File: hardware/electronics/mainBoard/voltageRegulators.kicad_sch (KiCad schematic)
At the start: 35 parts, among them U14 TPS65268-Q1

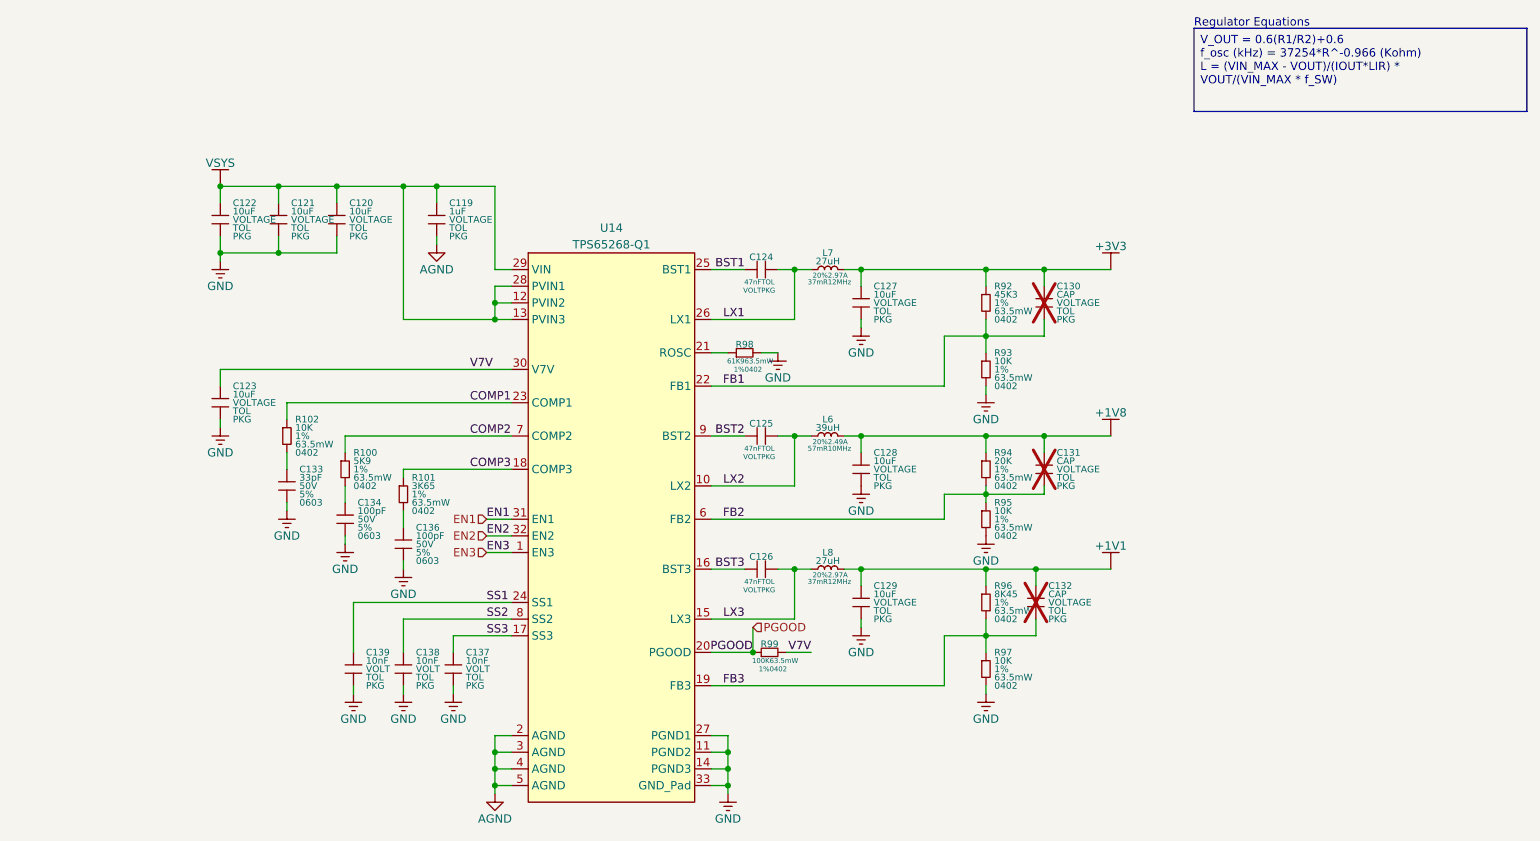
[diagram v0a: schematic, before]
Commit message: fixed vreg from WEBENCH results
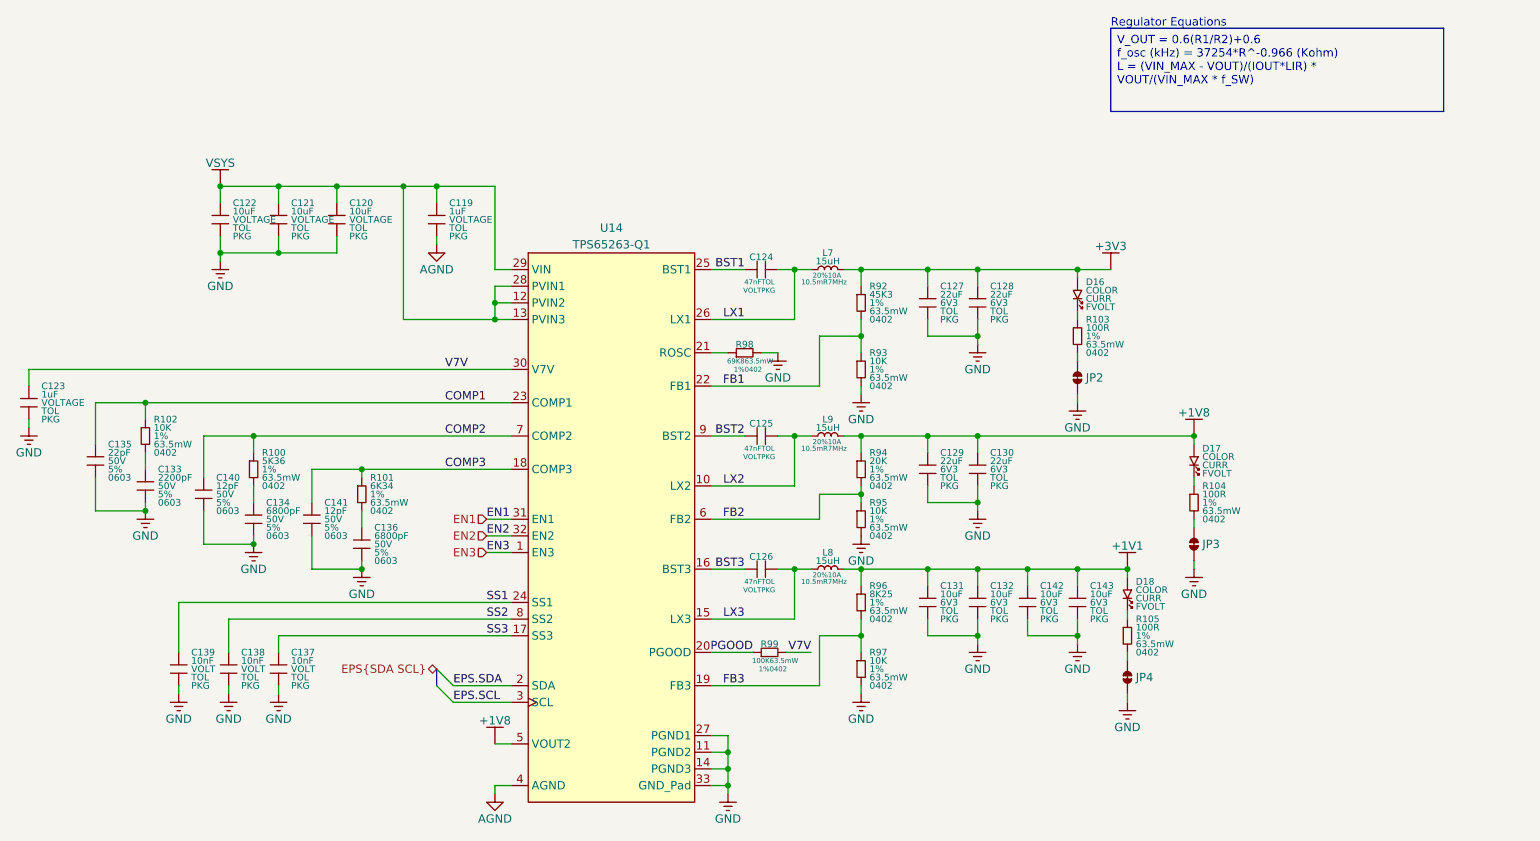
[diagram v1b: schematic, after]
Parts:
- removed L6: 39uH, symbol lib_sch:L_horizontal
- removed U14: TPS65268-Q1, symbol lib_sch:TPS65268-Q1
- added C135: 22pF, symbol lib_sch:C
- added C140, C141: 12pF, symbol lib_sch:C
- added C142, C143: 10uF, symbol lib_sch:C
- added D16, D17, D18: ~, symbol lib_sch:LED
- added JP2, JP3, JP4: ~, symbol .DS-Jumpers:Jumper_2_Bridged
- added L9: 15uH, symbol lib_sch:L_horizontal
- added R103, R104, R105: 100R, symbol lib_sch:R
- added U14: TPS65263-Q1, symbol lib_sch:TPS65263-Q1
- C123: value 10uF -> 1uF
- C127, C128, C129: value 10uF -> 22uF; Voltage Rating VOLTAGE -> 6V3
- C130: value CAP -> 22uF; Voltage Rating VOLTAGE -> 6V3; now fitted
- C131, C132: value CAP -> 10uF; Voltage Rating VOLTAGE -> 6V3; now fitted
- C133: value 33pF -> 2200pF; DKPN 478-KAM15ACG1H330JTCT-ND -> (none); MPN KAM15ACG1H330JT -> (none)
- C134, C136: value 100pF -> 6800pF; DKPN 478-KAM15ACG1H101JTCT-ND -> (none); MPN KAM15ACG1H101JT -> (none)
- L7, L8: value 27uH -> 15uH; Current Rating 2.97A -> 10A; DC Resistance 37mR -> 10.5mR; DKPN 732-4116-1-ND -> 732-10717-1-ND; MPN 744771127 -> 74439370150; Resonant Frequency 12MHz -> 7MHz
- R100: value 5K9 -> 5K36; DKPN 541-5.90KLCT-ND -> CRCW04025K36FKED; MPN CRCW04025K90FKED -> CRCW04025K36FKED
- R101: value 3K65 -> 6K34; DKPN 541-3.65LLCT-ND -> 541-6.34KLCT-ND; MPN CRCW04023R65FKED -> CRCW04026K34FKED
- R92: DKPN (none) -> 541-45.3KLCT-ND; MPN (none) -> CRCW040245K3FKED; Manufacturer (none) -> Vishay Dale
- R94: DKPN (none) -> 541-20.0KLCT-ND; MPN (none) -> CRCW040220K0FKED; Manufacturer (none) -> Vishay Dale
- R96: value 8K45 -> 8K25; DKPN (none) -> 541-8.25KLCT-ND; MPN (none) -> CRCW04028K25FKED; Manufacturer (none) -> Vishay Dale
- R98: value 61K9 -> 69K8; DKPN (none) -> 541-69.8KLCT-ND; MPN (none) -> CRCW040269K8FKED; Manufacturer (none) -> Vishay Dale
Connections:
- net +1V1: now also C131.1, C142.1, C143.1, D18.1; no longer C129.1
- net +1V8: now also C129.1, C130.1, D17.1, L9.2, U14.5 (VOUT2); no longer C128.1, C131.1
- net +3V3: now also C128.1, D16.1; no longer C130.1
- net AGND: now also U14.4 (AGND)
- net BST1: now also U14.25 (BST1)
- net BST2: now also U14.9 (BST2)
- net BST3: now also U14.16 (BST3)
- net COMP1: now also C135.1, U14.23 (COMP1)
- net COMP2: now also C140.1, U14.7 (COMP2)
- net COMP3: now also C141.1, U14.18 (COMP3)
- net EN1: now also U14.31 (EN1)
- net EN2: now also U14.32 (EN2)
- net EN3: now also U14.1 (EN3)
- net FB1: now also U14.22 (FB1); no longer C130.2
- net FB2: now also U14.6 (FB2); no longer C131.2
- net FB3: now also U14.19 (FB3); no longer C132.2
- net GND: now also C130.2, C131.2, C132.2, C135.2, C140.2, C141.2, C142.2, C143.2, JP2.1, JP3.1, JP4.1, U14.11 (PGND2), U14.14 (PGND3), U14.27 (PGND1), U14.33 (GND_Pad)
- net LX1: now also U14.26 (LX1)
- net LX2: now also L9.1, U14.10 (LX2)
- net LX3: now also U14.15 (LX3)
- net PGOOD: now also U14.20 (PGOOD)
- net SS1: now also U14.24 (SS1)
- net SS2: now also U14.8 (SS2)
- net SS3: now also U14.17 (SS3)
- net V7V: now also U14.30 (V7V)
- net VSYS: now also U14.12 (PVIN2), U14.13 (PVIN3), U14.28 (PVIN1), U14.29 (VIN)
- net at R98.1: now also U14.21 (ROSC)
- new net: JP2.2, R103.2
- new net: D17.2, R104.1
- new net: JP3.2, R104.2
- new net: D16.2, R103.1
- new net: D18.2, R105.1
- new net: JP4.2, R105.2
- new net EPS.SCL: U14.3 (SCL)
- new net EPS.SDA: U14.2 (SDA)
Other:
- title: (none) -> Voltage Regulators
- moved on the sheet: C123, C127, C133, C134, C136, C137, C138, C139, R100, R101, R102, R92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

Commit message: added new 4-channel vreg
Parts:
- added C114: 3.3uF, symbol lib_sch:C
- added C115: 4.7uF, symbol lib_sch:C
- added C150, C162, C163, C164, C165, C166, C169, C173, C174, C175: 10uF, symbol lib_sch:C
- added C151: 4.7pF, symbol lib_sch:C
- added C157, C158, C159, C160: 6800pF, symbol lib_sch:C_horizontal
- added C161, C170, C177, C178: 100nF, symbol lib_sch:C
- added C167, C168: 5600pF, symbol lib_sch:C
- added C171: 12nF, symbol lib_sch:C
- added C172: 33nF, symbol lib_sch:C
- added L10: 100uH, symbol lib_sch:L_horizontal
- added L11: 47uH, symbol lib_sch:L_horizontal
- added L5: 180uH, symbol lib_sch:L_horizontal
- added L6: 33uH, symbol lib_sch:L_horizontal
- added R114: 37K4, symbol lib_sch:R
- added R115, R84, R86, R88: 100K, symbol lib_sch:R
- added R116: 34K8, symbol lib_sch:R
- added R117: 34K, symbol lib_sch:R
- added R118: 6K04, symbol lib_sch:R
- added R119: 3K57, symbol lib_sch:R
- added R78, R79, R82: 10K, symbol lib_sch:R
- added R80: 576K, symbol lib_sch:R
- added R81: 383K, symbol lib_sch:R
- added R83: 22K1, symbol lib_sch:R
- added R85: 340K, symbol lib_sch:R
- added R87: 137K, symbol lib_sch:R
- added U2: TPS65400, symbol .DS-PMIC:TPS65400
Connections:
- net +1V1: now also C166.1, L5.2, R114.1
- net +1V8: now also C174.1, L10.2, R87.1
- net +3V3: now also C163.1, C164.1, C165.1, L6.2, R85.1
- net AGND: now also C151.2, R81.2, U2.21 (AGND)
- net COMP1: now also R116.1, R117.1, R118.1, R119.1, U2.46 (COMP1)
- net COMP2: now also U2.15 (COMP2)
- net COMP3: now also U2.25 (COMP3)
- net EPS.SCL: now also U2.42 (SDA)
- net EPS.SDA: now also U2.43 (SCL)
- net GND: now also C114.2, C115.2, C150.2, C157.1, C158.1, C159.1, C160.1, C162.2, C163.2, C164.2, C165.2, C166.2, C167.2, C168.2, C169.2, C171.2, C172.2, C173.2, C174.2, C175.2, R115.2, R83.2, R84.2, R86.2, R88.2, U2.49 (GND_PAD), U2.7 (PGND1), U2.8 (PGND2)
- net VSYS: now also C173.1, C175.1, U2.22 (VIN), U2.30 (PVIN3), U2.31 (PVIN4), U2.5 (PVIN1), U2.6 (PVIN2)
- new net: R80.2, R84.1, U2.47 (VFB1)
- new net: C170.2, L6.1, U2.10 (SW2), U2.11 (SW2), U2.9 (SW2)
- new net: C178.1, U2.33 (CB4)
- new net: C178.2, L5.1, U2.32 (SW4)
- new net: C160.2, U2.37 (SS4/PG4)
- new net: C172.1, R119.2
- new net: C171.1, R118.2
- new net: R87.2, R88.1, U2.26 (VFB3)
- new net: R85.2, R86.1, U2.14 (VFB2)
- new net: C168.1, R117.2
- new net: C158.2, U2.16 (SS2/PG2)
- new net: C177.2, L10.1, U2.29 (SW3)
- new net: C177.1, U2.28 (CB3)
- new net: C167.1, R116.2
- new net: C151.1, R81.1, U2.40 (RCLOCK_SYNC)
- new net: R114.2, R115.1, U2.35 (VFB4)
- new net: C161.2, L11.1, U2.2 (SW1), U2.3 (SW1), U2.4 (SW1)
- new net: R83.1, U2.38 (I2CADDR)
- new net: R79.2, U2.41 (I2CALERT)
- new net: C170.1, U2.12 (CB2)
- new net: C159.2, U2.24 (SS3/PG3)
- new net: C161.1, U2.1 (CB1)
- new net: R78.2, U2.17 (PGOOD)
- new net: C157.2, U2.45 (SS1/PG1)
- new net +5V: C162.1, C169.1, L11.2, R80.1
- new net COMP4: U2.36 (COMP4)
- new net VDDA: C115.1, U2.19 (VDDA)
- new net VDDD: C114.1, R78.1, R79.1, R82.1, U2.20 (VDDD)
- new net VDDG: C150.1, U2.18 (VDDG)
- new net VREG.EN1: U2.48 (ENSW1/ENSEQ)
- new net VREG.EN2: U2.13 (ENSW2)
- new net VREG.EN3: U2.27 (ENSW3)
- new net VREG.EN4: U2.34 (ENSW4)
- new net VREG.RST: R82.2, U2.39 (RST_N)
- no-connect marks 0 -> 2
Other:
- note added: "VFB=0.74V"
- note added: "VFB=0.75V"
- note added: "VFB=0.76V"
- note added: "VFB=0.8V"
- moved on the sheet: C119, C120, C121, C122, C123, C124, C125, C126, C127, C128, C129, C130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

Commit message: added regulators for 5V, 3V3, 1V8, and 1V1
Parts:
- removed C114: 3.3uF, symbol lib_sch:C
- removed C115: 4.7uF, symbol lib_sch:C
- removed C119, C123: 1uF, symbol lib_sch:C
- removed C120, C121, C122, C131, C132, C142, C143, C150, C162, C163, C164, C165, C166, C169, C173, C174, C175: 10uF, symbol lib_sch:C
- removed C124, C125, C126: 47nF, symbol lib_sch:C_horizontal
- removed C127, C128, C129, C130: 22uF, symbol lib_sch:C
- removed C133: 2200pF, symbol lib_sch:C
- removed C134, C136: 6800pF, symbol lib_sch:C
- removed C135: 22pF, symbol lib_sch:C
- removed C137, C138, C139: 10nF, symbol lib_sch:C
- removed C140, C141: 12pF, symbol lib_sch:C
- removed C151: 4.7pF, symbol lib_sch:C
- removed C157, C158, C159, C160: 6800pF, symbol lib_sch:C_horizontal
- removed C161, C170, C177, C178: 100nF, symbol lib_sch:C
- removed C167, C168: 5600pF, symbol lib_sch:C
- removed C171: 12nF, symbol lib_sch:C
- removed C172: 33nF, symbol lib_sch:C
- removed D16, D17, D18: ~, symbol lib_sch:LED
- removed JP2, JP3, JP4: ~, symbol .DS-Jumpers:Jumper_2_Bridged
- removed L10: 100uH, symbol lib_sch:L_horizontal
- removed L11: 47uH, symbol lib_sch:L_horizontal
- removed L5: 180uH, symbol lib_sch:L_horizontal
- removed L6: 33uH, symbol lib_sch:L_horizontal
- removed L7, L8, L9: 15uH, symbol lib_sch:L_horizontal
- removed R100: 5K36, symbol lib_sch:R
- removed R101: 6K34, symbol lib_sch:R
- removed R102, R78, R79, R82, R93, R95, R97: 10K, symbol lib_sch:R
- removed R103, R104, R105: 100R, symbol lib_sch:R
- removed R114: 37K4, symbol lib_sch:R
- removed R115, R84, R86, R88: 100K, symbol lib_sch:R
- removed R116: 34K8, symbol lib_sch:R
- removed R117: 34K, symbol lib_sch:R
- removed R118: 6K04, symbol lib_sch:R
- removed R119: 3K57, symbol lib_sch:R
- removed R80: 576K, symbol lib_sch:R
- removed R81: 383K, symbol lib_sch:R
- removed R83: 22K1, symbol lib_sch:R
- removed R85: 340K, symbol lib_sch:R
- removed R87: 137K, symbol lib_sch:R
- removed R92: 45K3, symbol lib_sch:R
- removed R94: 20K, symbol lib_sch:R
- removed R96: 8K25, symbol lib_sch:R
- removed R98: 69K8, symbol lib_sch:R_horizontal
- removed R99: 100K, symbol lib_sch:R_horizontal
- removed U14: TPS65263-Q1, symbol lib_sch:TPS65263-Q1
- removed U2: TPS65400, symbol .DS-PMIC:TPS65400
- added C113: 24pF, symbol lib_sch:C
- added C176, C179, C180, C181: 100uF, symbol lib_sch:C
- added C182: 2.2uF, symbol lib_sch:C
- added C183: 100nF, symbol lib_sch:C
- added C184, C185, C188, C189: 4.7uF, symbol lib_sch:C
- added C186, C187: 1uF, symbol lib_sch:C
- added C190, C192, C193, C194, C195: 10uF, symbol lib_sch:C
- added C191, C196, C197: 22uF, symbol lib_sch:C
- added L12: 10uH, symbol lib_sch:L_horizontal
- added L13: 1uH, symbol lib_sch:L_horizontal
- added L14: 74439358010, symbol lib_sch:L_horizontal
- added L15: VAL, symbol lib_sch:L_horizontal
- added R10: 24K3, symbol lib_sch:R
- added R11: 49K9, symbol lib_sch:R
- added R12: 10R, symbol lib_sch:R_horizontal
- added R120, R125, R15: 100K, symbol lib_sch:R
- added R121: 22K1, symbol lib_sch:R
- added R122: 249K, symbol lib_sch:R
- added R123: 34K, symbol lib_sch:R
- added R124: 100K, symbol lib_sch:R_horizontal
- added R13, R9: 10K, symbol lib_sch:R
- added R14: 200K, symbol lib_sch:R
- added R27, R28: 499K, symbol lib_sch:R
- added R29: 82K5, symbol lib_sch:R
- added R8: 56K, symbol lib_sch:R
- added U16: TPS543B25, symbol .DS-PMIC:TPS543B25
- added U17, U18: TPS62A01, symbol .DS-PMIC:TPS62A0x
- added U19: TPS629206, symbol .DS-PMIC:TPS629206
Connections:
- net +1V1: now also C193.1, C194.1, C195.1, L14.2, R29.1
- net +1V8: now also C191.1, L13.2, R14.1
- net +3V3: now also C113.1, C176.1, C179.1, C180.1, C190.1, C192.1, L12.2, R125.1, R27.1, R28.1, R8.1, U17.3 (VIN), U18.3 (VIN)
- net +5V: now also C197.1, L15.2, R122.1, U19.3 (VOS)
- net AGND: now also C183.2, R10.2, R11.2, U16.1 (AGND)
- net GND: now also C176.2, C179.2, C180.2, C182.2, C184.2, C185.2, C186.2, C187.2, C188.2, C189.2, C190.2, C191.2, C192.2, C193.2, C194.2, C195.2, C196.2, C197.2, R120.2, R121.2, R123.2, R15.2, R9.2, U16.14 (GOSNS), U16.16 (PGND), U16.17 (PGND), U16.5 (PGND), U16.8 (PGND), U17.1 (GND), U18.1 (GND), U19.5 (GND)
- net VSYS: now also C184.1, C185.1, C186.1, C187.1, C188.1, C189.1, C196.1, U16.4 (VIN), U16.9 (VIN), U19.6 (VIN)
- new net BOOT_3V3: C181.1, U16.7 (BOOT)
- new net EN_1V1: U18.4 (EN)
- new net EN_1V8: U17.4 (EN)
- new net EN_3V3: U16.10 (EN)
- new net EN_5V: U19.7 (EN)
- new net FB_1V1: R120.1, R29.2, U18.5 (FB)
- new net FB_1V8: R14.2, R15.1, U17.5 (FB)
- new net FB_3V3: C113.2, R8.2, R9.1, U16.15 (FB)
- new net FB_5V: R122.2, R123.1, U19.1 (FB)
- new net FSEL: R10.1, U16.12 (SYNC)
- new net MODE: R121.1, U19.8 (MODE)
- new net MSEL: R11.1, U16.13 (MSEL)
- new net PG_1V1: R28.2, U18.6 (PG)
- new net PG_1V8: R27.2, U17.6 (PG)
- new net PG_3V3: R13.2, U16.11 (PG)
- new net PG_5V: R124.1, R124.2, R125.2, U19.2 (PG)
- new net SW_1V1: L14.1, U18.2 (SW)
- new net SW_1V8: L13.1, U17.2 (SW)
- new net SW_3V3: C181.2, L12.1, U16.6 (SW)
- new net SW_5V: L15.1, U19.4 (SW)
- new net VCC_3V3: C183.1, R12.2, R13.1, U16.2 (VCC)
- new net VDRV: C182.1, R12.1, U16.3 (VDRV)
- no-connect marks 2 -> 1
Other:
- note added: "+1V1 Voltage Regulator"
- note added: "+1V8 Voltage Regulator"
- note added: "+3V3 Voltage Regulator"
- note added: "+5V Voltage Regulator"
- note removed: "Regulator Equations"
- note removed: "VFB=0.74V"
- note removed: "VFB=0.75V"
- note removed: "VFB=0.76V"
- note removed: "VFB=0.8V"
